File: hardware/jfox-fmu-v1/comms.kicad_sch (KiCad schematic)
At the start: 6 parts, among them J30 USB-C, J31 microSD, U30 TCAN332, U31 TCAN332

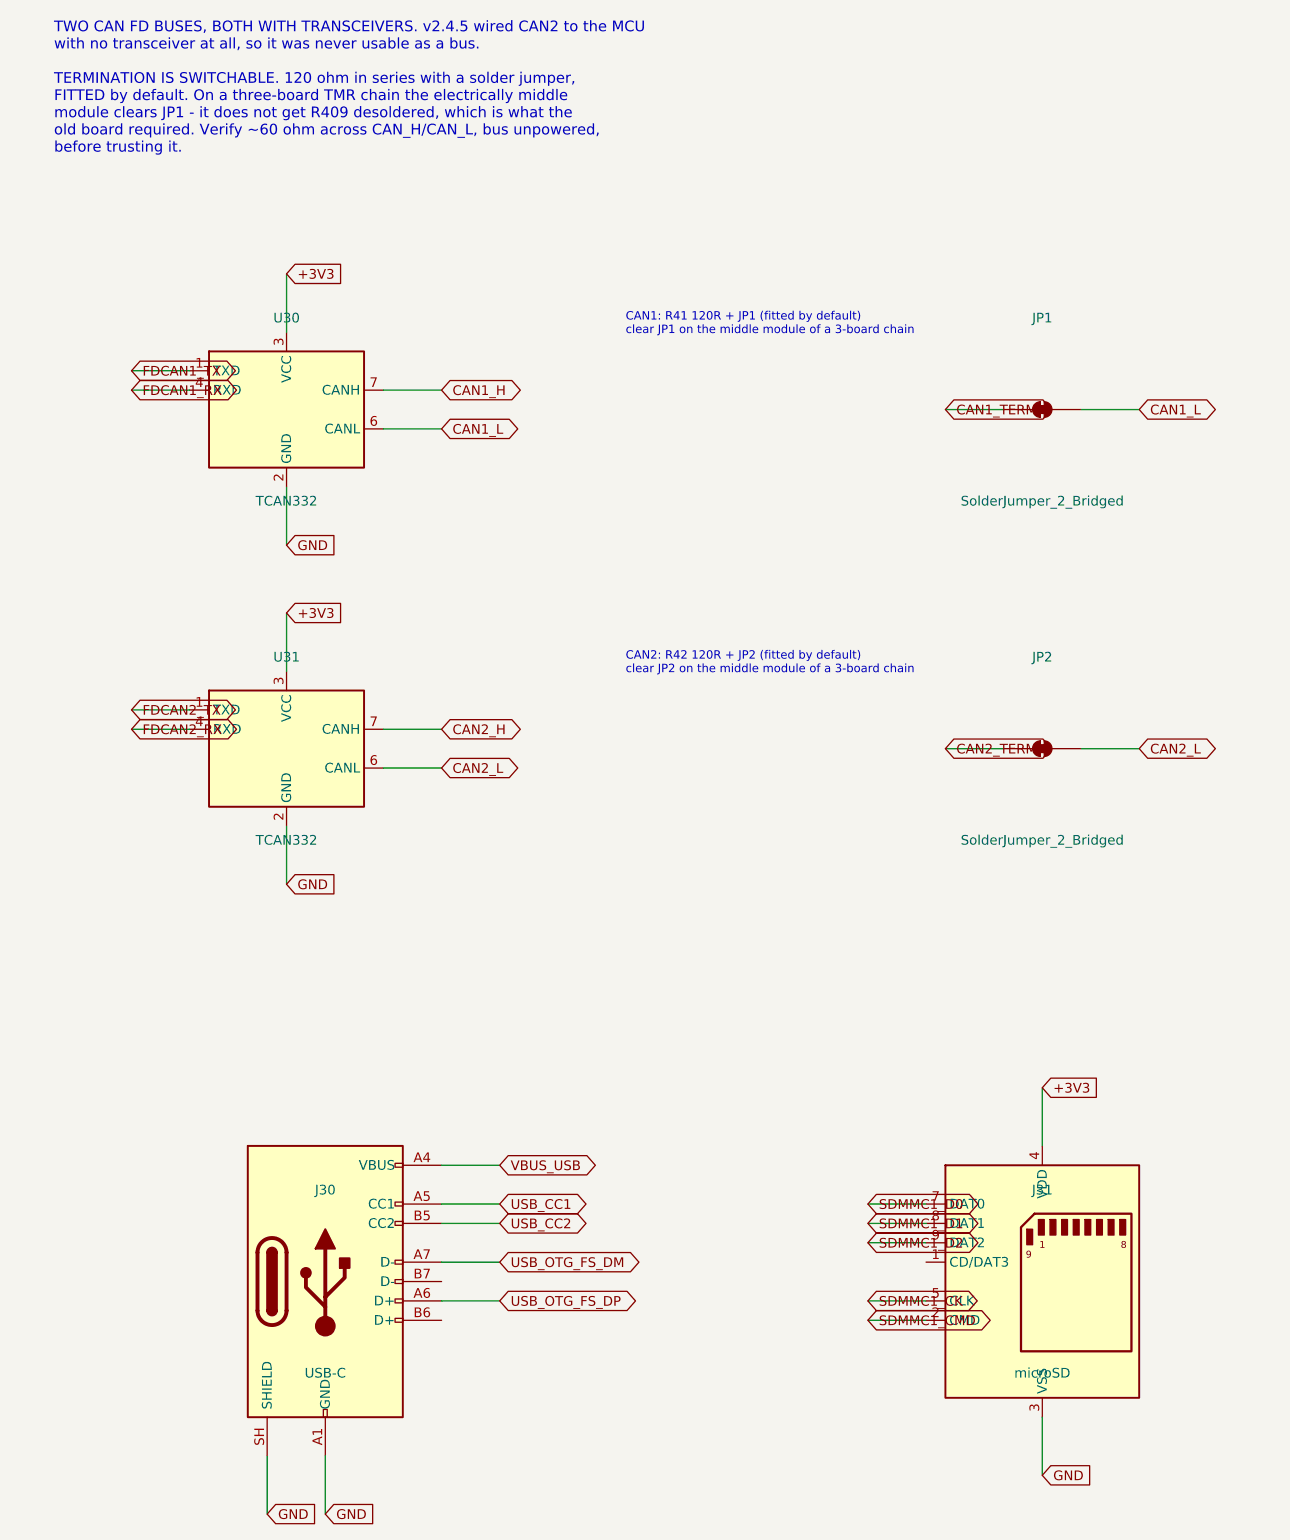
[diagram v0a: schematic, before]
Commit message: Isolated CAN FD, and the short it took a bisect to find
CAN redundancy is resolved by using Cyphal. FDCAN1 and FDCAN2 become two
redundant Cyphal/CAN interfaces on two independent isolated buses.

That is not the compromise it looked like. Cyphal handles redundancy in the
protocol: the specification defines redundant transport groups where a node
publishes on every interface and the receiver deduplicates, per frame or per
transfer. libcanard gives each redundant interface its own TX queue for
exactly this. So two controllers is the arrangement Cyphal is built around,
and it buys controller-level redundancy rather than the isolator-level
redundancy that keeping two separate buses would have given. The "four
controllers needed, two available" constraint dissolves rather than binds.

Better still, if wanted later: Cyphal supports heterogeneous redundancy, so a
Cyphal/CAN interface paired with Cyphal/UDP would give dissimilar transport
redundancy - the same argument that puts three IMUs from two vendors here.

U30/U31 become ISOW1044: isolated CAN FD with an integrated isolated DC-DC, so
each bus gets its own supply domain without a separate converter. Two
datasheet shorts that are easy to miss and both mandatory (SLLSFF7A table
7-1): GNDIO and GND1 are not internally connected, and VISOOUT/VSIN/VISOIN are
one node. EN/FLT is wired as the fault output with a 10k pull-up, because a
redundant link whose failure is silent is not redundant.

And the bug. Swapping an 8-pin TCAN332 for a 20-pin ISOW1044 while leaving the
row pitch at 44.45 mm overlapped the two transceivers - the ISOW1044 spans
35.56 mm and 50.8 mm with its stubs. Their stub ends coincided and merged the
rails. The netlist came out with no GND net and no +5V net at all: 171 pins on
+3V3, ground shorted to the supply across the entire board.

Nothing caught it. ERC does not object to a short - it is well-formed. The
page-fit and footprint checks passed. Even "all MCU supply pins sit on their
rail" passed, beca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
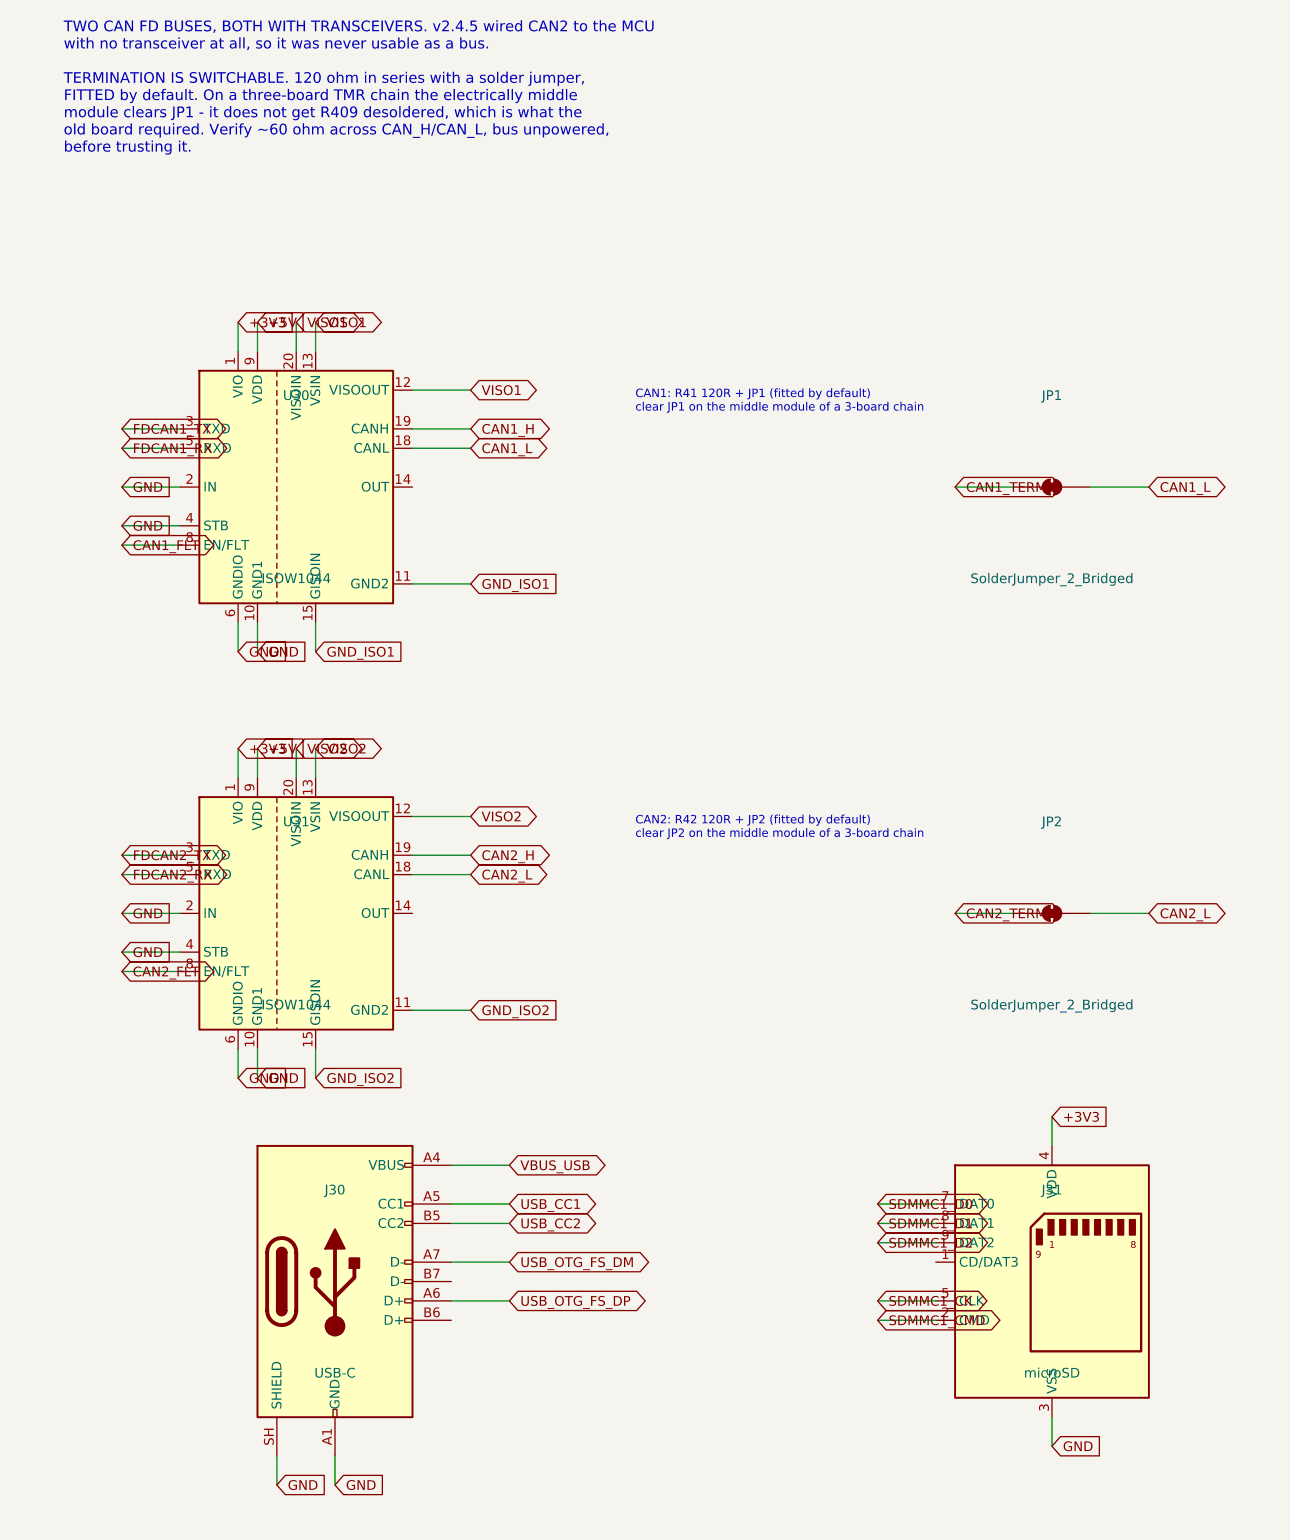
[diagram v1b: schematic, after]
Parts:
- removed U30, U31: TCAN332, Package_SO:SOIC-8_3.9x4.9mm_P1.27mm, symbol Interface_CAN_LIN:TCAN332
- added U30, U31: ISOW1044, Package_SO:SOIC-20W_7.5x12.8mm_P1.27mm, symbol Interface_CAN_LIN:ISOW1044
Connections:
- net +3V3: now also U30.1 (VIO), U31.1 (VIO)
- net CAN1_H: now also U30.19 (CANH)
- net CAN1_L: now also U30.18 (CANL)
- net CAN2_H: now also U31.19 (CANH)
- net CAN2_L: now also U31.18 (CANL)
- net FDCAN1_RX: now also U30.5 (RXD)
- net FDCAN1_TX: now also U30.3 (TXD)
- net FDCAN2_RX: now also U31.5 (RXD)
- net FDCAN2_TX: now also U31.3 (TXD)
- net GND: now also U30.10 (GND1), U30.2 (IN), U30.4 (STB), U30.6 (GNDIO), U31.10 (GND1), U31.2 (IN), U31.4 (STB), U31.6 (GNDIO)
- new net +5V: U30.9 (VDD), U31.9 (VDD)
- new net CAN1_FLT: U30.8 (EN/FLT)
- new net CAN2_FLT: U31.8 (EN/FLT)
- new net GND_ISO1: U30.11 (GND2), U30.15 (GISOIN), U30.16 (GISOIN), U30.17 (GISOIN)
- new net GND_ISO2: U31.11 (GND2), U31.15 (GISOIN), U31.16 (GISOIN), U31.17 (GISOIN)
- new net VISO1: U30.12 (VISOOUT), U30.13 (VSIN), U30.20 (VISOIN)
- new net VISO2: U31.12 (VISOOUT), U31.13 (VSIN), U31.20 (VISOIN)

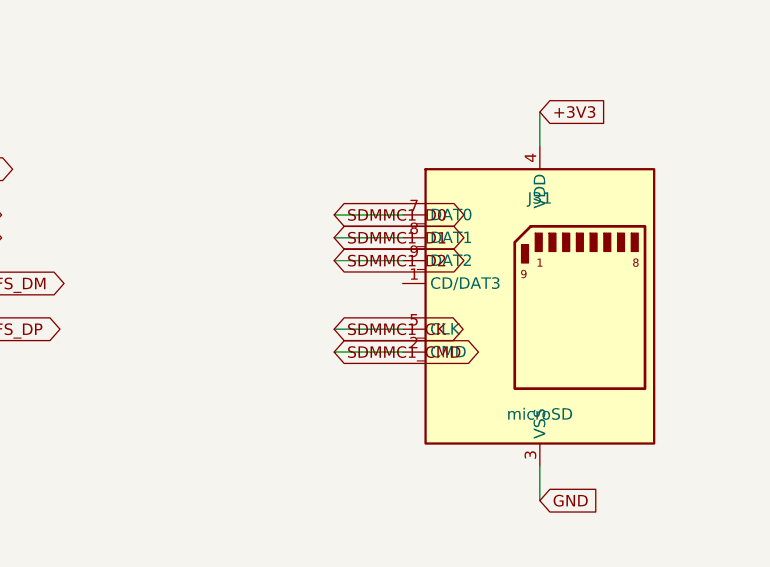
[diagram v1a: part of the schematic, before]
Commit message: Five connections that went nowhere, and the pin name that hid one
None of these were visible as failures. Every one was a wire drawn to a name
that did not exist, which KiCad accepts silently.

wire_part matches by pin NAME. Four keys in the comms sheet matched nothing:

  "DAT3/CS"  the microSD symbol's pin is "CD/DAT3", so SDMMC1_D3 reached the
             MCU and stopped. The card would have run in 1-bit mode at best.
  "DET"      this symbol has no card-detect pin at all, so SD_DETECT had no
             source. Recorded rather than faked - it needs a socket symbol
             that exposes CD.
  "VSS2"     does not exist on this symbol.
  "SBU1/2"   do not exist on the USB-C symbol.

PC2 is the one worth remembering. On this package PC2 and PC3 exist only as
PC2_C and PC3_C - the analog-switch-capable balls. plan_pinout works from the
chip's alternate-function table, which calls them PC2 and PC3, so the lookup
missed and the allocated signal went nowhere. Aliased in both the generator
and the checker, which is what surfaced it: the check reported "symbol has no
pin named PC2" the moment the allocation grew enough to reach that pin.

Four parts that were missing outright, each leaving a function non-functional:

  R9/R10   5.1k on USB CC1/CC2. Without them the port is not a USB-C sink and
           no host will enumerate it. The CC pins reached the connector and
           nothing else.
  R11/R12  VBUS sense divider. VBUS_SENSE reached an ADC pin with nothing
           driving it. 10k/10k puts 5.25 V at 2.63 V, inside the reference.
  R13-R16  pull-ups on the four load-switch fault outputs, which are open
           drain and were unreadable without them.

And ten status signals now reach the MCU that previously reached nothing:
BRICK_VALID, SERVO_VALID, USB_VALID, PG_3V3, the four rail fault flags and
both isolator fault outputs. The board could not previously tell whether its
power source was valid, whether a sensor rail had tripped, or whether an
isolated 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
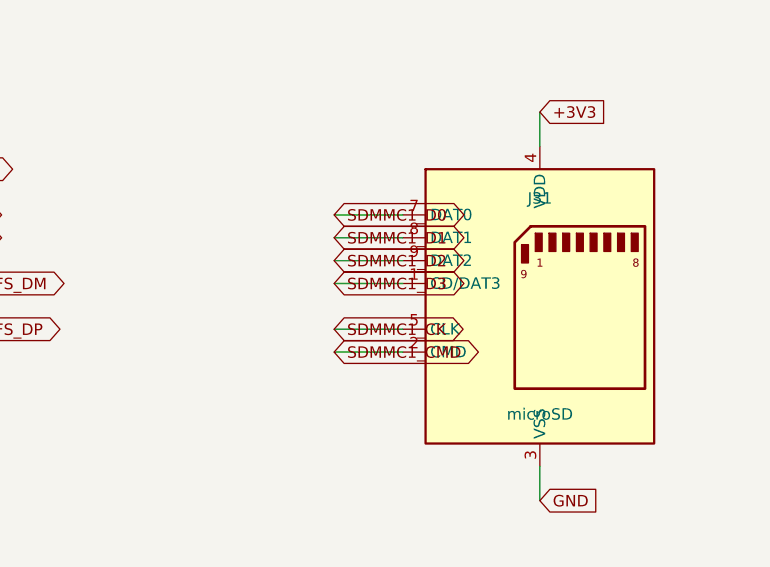
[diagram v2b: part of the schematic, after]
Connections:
- net SDMMC1_D3: now reaches J31.1 (CD/DAT3)
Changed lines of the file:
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@@
 		(instances
 			(project "jfox-fmu"
-				(path "/c73b6849-d5d1-49b3-8b87-c3d36fa2a794"
+				(path "/65247fae-fc4d-48b6-84aa-993fae0d1b94"
 					(reference "U30")
 					(unit 1)
@@
 		(instances
 			(project "jfox-fmu"
-				(path "/c73b6849-d5d1-49b3-8b87-c3d36fa2a794"
+				(path "/65247fae-fc4d-48b6-84aa-993fae0d1b94"
 					(reference "JP1")
 					(unit 1)
@@
 		(instances
 			(project "jfox-fmu"
-				(path "/c73b6849-d5d1-49b3-8b87-c3d36fa2a794"
+				(path "/65247fae-fc4d-48b6-84aa-993fae0d1b94"
 					(reference "U31")
 					(unit 1)
@@
 		(instances
 			(project "jfox-fmu"
-				(path "/c73b6849-d5d1-49b3-8b87-c3d36fa2a794"
+				(path "/65247fae-fc4d-48b6-84aa-993fae0d1b94"
 					(reference "JP2")
 					(unit 1)
@@
 		(instances
 			(project "jfox-fmu"
-				(path "/c73b6849-d5d1-49b3-8b87-c3d36fa2a794"
+				(path "/65247fae-fc4d-48b6-84aa-993fae0d1b94"
 					(reference "J30")
 					(unit 1)
@@
 		(instances
 			(project "jfox-fmu"
-				(path "/c73b6849-d5d1-49b3-8b87-c3d36fa2a794"
+				(path "/65247fae-fc4d-48b6-84aa-993fae0d1b94"
 					(reference "J31")
 					(unit 1)
@@
 		)
 	)
+	(wire
+		(pts
+			(xy 146.05 176.53) (xy 138.43 176.53)
+		)
+		(stroke
+			(width 0)
+			(type default)
+		)
+	)
+	(global_label "SDMMC1_D3"
+		(shape bidirectional)
+		(at 138.43 176.53 0)
+		(fields_autoplaced yes)
+		(effects
+			(font
+				(size 1.27 1.27)
+			)
+			(justify left)
+		)
+	)
